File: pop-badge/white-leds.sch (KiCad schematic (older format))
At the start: 122 parts, among them Q1 BC818

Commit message: much more layouting
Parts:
- removed D51, D52, D53, D54, D55, D56, D57, D58, D59, D60: LED, LED_SMD:LED_0603_1608Metric, symbol Device:LED
- removed R51, R52, R53, R54, R55, R56, R57, R58, R59, R60: 100, Resistor_SMD:R_0603_1608Metric_Pad1.05x0.95mm_HandSolder, symbol Device:R
- renumbered R61 to R51

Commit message: routing mostly done
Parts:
- D1, D10, D11, D12, D13, D14, D15, D16, D17, D18, D19, D2, D20, D21, D22, D23, D24, D25, D26, D27, D28, D29, D3, D30, D31, D32, D33, D34, D35, D36, D37, D38, D39, D4, D40, D41, D42, D43, D44, D45, D46, D47, D48, D49, D5, D50, D6, D7, D8, D9: JLC (none) -> C115461
- R1, R10, R11, R12, R13, R14, R15, R16, R17, R18, R19, R2, R20, R21, R22, R23, R24, R25, R26, R27, R28, R29, R3, R30, R31, R32, R33, R34, R35, R36, R37, R38, R39, R4, R40, R41, R42, R43, R44, R45, R46, R47, R48, R49, R5, R50, R51, R6, R7, R8, R9: JLC (none) -> 0603

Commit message: different BJT again
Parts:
- Q1: footprint Package_TO_SOT_SMD:SOT-416 -> Package_TO_SOT_SMD:SOT-23
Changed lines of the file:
@@
 F 0 "Q1" H 1791 5746 50  0000 L CNN
 F 1 "BC818" H 1791 5655 50  0000 L CNN
-F 2 "Package_TO_SOT_SMD:SOT-416" H 1800 5625 50  0001 L CIN
+F 2 "Package_TO_SOT_SMD:SOT-23" H 1800 5625 50  0001 L CIN
 F 3 "https://www.fairchildsemi.com/datasheets/BC/BC818.pdf" H 1600 5700 50  0001 L CNN
 	1    1600 5700

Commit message: use 200 ohm current limiting resistor for LED
To have more headroom without bringing BJT to its limits.

Calculation basis:

 V_CE 0.6V max
 LTW-C193SN5 10mA at 3.15V, from chart ~ 5mA at 3V

7mA at 200 Ohm = 1.4V voltage drop

worst case 5V - 0.5V - 1.4V = 3.1V ~ 7mA at LED according to LED IV chart
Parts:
- Q1: value BC818 -> S9013; JLC (none) -> C6749
- R1, R10, R11, R12, R13, R14, R15, R16, R17, R18, R19, R2, R20, R21, R22, R23, R24, R25, R26, R27, R28, R29, R3, R30, R31, R32, R33, R34, R35, R36, R37, R38, R39, R4, R40, R41, R42, R43, R44, R45, R46, R47, R48, R49, R5, R50, R6, R7, R8, R9: value 100 -> 200

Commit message: use proper pin connector and expose LEDw- on connector
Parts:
- removed Q1: S9013, Package_TO_SOT_SMD:SOT-23, symbol Transistor_BJT:BC818
- removed R51: 4k7, Resistor_SMD:R_0603_1608Metric_Pad1.05x0.95mm_HandSolder, symbol Device:R
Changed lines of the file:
@@
 Text GLabel 1800 4850 2    50   Input ~ 0
 LEDw+
-$Comp
-L Device:R R51
-U 1 1 615A4B23
-P 1250 5700
-F 0 "R51" V 1043 5700 50  0000 C CNN
-F 1 "4k7" V 1134 5700 50  0000 C CNN
-F 2 "Resistor_SMD:R_0603_1608Metric_Pad1.05x0.95mm_HandSolder" V 1180 5700 50  0001 C CNN
-F 3 "~" H 1250 5700 50  0001 C CNN
-F 4 "0603" H 1250 5700 50  0001 C CNN "JLC"
-	1    1250 5700
-	0    1    1    0
-$EndComp
-Text HLabel 1100 5700 0    50   Input ~ 0
-LEDwMCU
 Text GLabel 700  1350 0    50   Input ~ 0
 LEDw-
@@
 	7050 1350 7400 1350
 Connection ~ 7050 1350
-Text GLabel 1800 5300 2    50   Input ~ 0
+Text GLabel 1800 5050 2    50   Input ~ 0
 LEDw-
-Wire Wire Line
-	1800 5300 1700 5300
-Wire Wire Line
-	1700 5300 1700 5500
-$Comp
-L Transistor_BJT:BC818 Q1
-U 1 1 616388C7
-P 1600 5700
-F 0 "Q1" H 1791 5746 50  0000 L CNN
-F 1 "S9013" H 1791 5655 50  0000 L CNN
-F 2 "Package_TO_SOT_SMD:SOT-23" H 1800 5625 50  0001 L CIN
-F 3 "" H 1600 5700 50  0001 L CNN
-F 4 "C6749" H 1600 5700 50  0001 C CNN "JLC"
-	1    1600 5700
-	1    0    0    -1
-$EndComp
-Text HLabel 1100 6050 0    50   Input ~ 0
-GND
 Text HLabel 1100 4850 0    50   Input ~ 0
 +5V
 Wire Wire Line
 	1100 4850 1800 4850
-Wire Wire Line
-	1700 5900 1700 6050
-Wire Wire Line
-	1100 6050 1700 6050
 $Comp
 L Device:LED D41
@@
 Connection ~ 5650 1550
 Connection ~ 5650 2150
+Text HLabel 1100 5050 0    50   Input ~ 0
+LEDw-
+Wire Wire Line
+	1100 5050 1800 5050
 $EndSCHEMATC

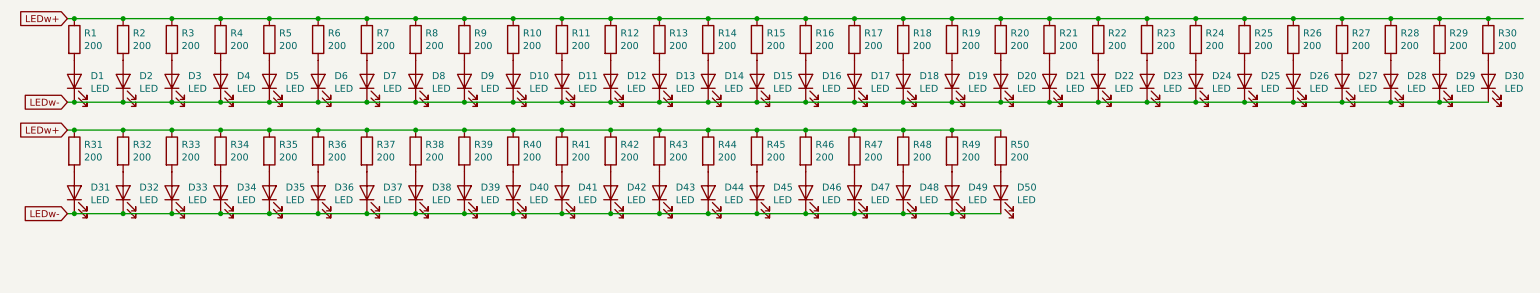
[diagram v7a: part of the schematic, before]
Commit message: renumber white leds
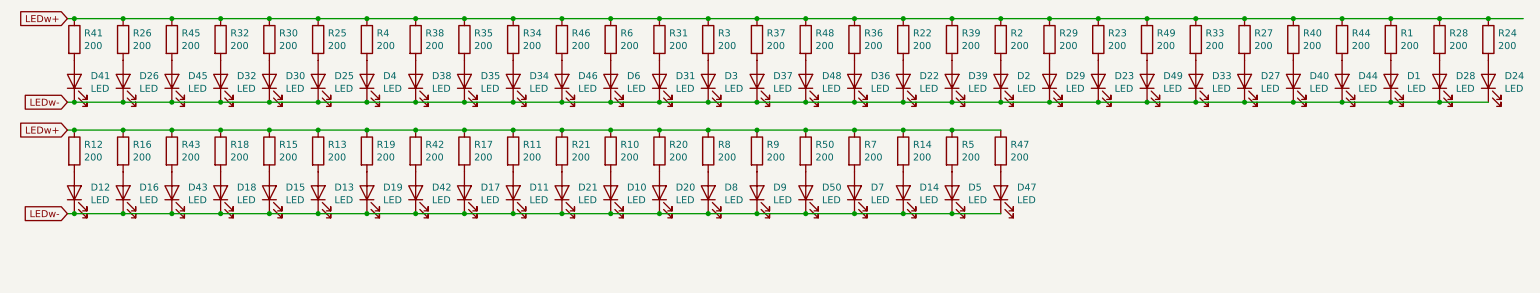
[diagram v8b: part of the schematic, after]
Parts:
- renumbered D28 to D1, D42 to D10, D40 to D11, D31 to D12, D36 to D13, D48 to D14, D35 to D15, D32 to D16, D39 to D17, D34 to D18, D37 to D19, D20 to D2, D43 to D20, D41 to D21, D18 to D22, D22 to D23, D30 to D24, D6 to D25, D2 to D26, D25 to D27, D29 to D28, D21 to D29, D14 to D3, D5 to D30, D13 to D31, D4 to D32, D24 to D33, D10 to D34, D9 to D35, D17 to D36, D15 to D37, D8 to D38, D19 to D39, D7 to D4, D26 to D40, D1 to D41, D38 to D42, D33 to D43, D27 to D44, D3 to D45, D11 to D46, D50 to D47, D16 to D48, D23 to D49, D49 to D5, D46 to D50, D12 to D6, D47 to D7, D44 to D8, D45 to D9, R28 to R1, R42 to R10, R40 to R11, R31 to R12, R36 to R13, R48 to R14, R35 to R15, R32 to R16, R39 to R17, R34 to R18, R37 to R19, R20 to R2, R43 to R20, R41 to R21, R18 to R22, R22 to R23, R30 to R24, R6 to R25, R2 to R26, R25 to R27, R29 to R28, R21 to R29, R14 to R3, R5 to R30, R13 to R31, R4 to R32, R24 to R33, R10 to R34, R9 to R35, R17 to R36, R15 to R37, R8 to R38, R19 to R39, R7 to R4, R26 to R40, R1 to R41, R38 to R42, R33 to R43, R27 to R44, R3 to R45, R11 to R46, R50 to R47, R16 to R48, R23 to R49, R49 to R5, R46 to R50, R12 to R6, R47 to R7, R44 to R8, R45 to R9
